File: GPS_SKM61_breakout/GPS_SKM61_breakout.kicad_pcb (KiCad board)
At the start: 2 copper layers, 49.5 x 38.1 mm, 2 parts, among them P1 CONN_01X06, U1 SKM61

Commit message: added gerbers for skm61
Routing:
- net Net-(P1-Pad6): track 0.00 -> 13.3 mm
- net Net-(P1-Pad5): track 0.00 -> 12.9 mm
- net Net-(P1-Pad1): track 0.00 -> 12.7 mm
- net Net-(P1-Pad4): track 0.00 -> 12.5 mm
- net Net-(P1-Pad2): track 0.00 -> 12.3 mm
- net Net-(P1-Pad3): track 0.00 -> 12.0 mm
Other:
- outline, holes or cut-outs redrawn
- net class Default: clearance 0.2 -> 0.8128; trace_width 0.25 -> 0.635; via_dia 0.6 -> 2.54; via_drill 0.4 -> 0.8128
- rule trace_clearance: 0.2 -> 0.8128
- rule trace_min: 0.2 -> 0.635
- rule via_min_drill: 0.3 -> 0.8128
- rule via_min_size: 0.4 -> 2.54
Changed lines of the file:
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@@
   (general
     (links 6)
-    (no_connects 6)
-    (area 0 0 0 0)
+    (no_connects 0)
+    (area 141.598867 93.904999 194.385001 132.155001)
     (thickness 1.6)
-    (drawings 4)
-    (tracks 0)
+    (drawings 8)
+    (tracks 25)
     (zones 0)
     (modules 2)
@@
   )
   (setup
-    (last_trace_width 0.25)
-    (trace_clearance 0.2)
+    (last_trace_width 1.778)
+    (user_trace_width 0.635)
+    (user_trace_width 0.762)
+    (user_trace_width 1.016)
+    (user_trace_width 1.27)
+    (user_trace_width 1.524)
+    (user_trace_width 1.778)
+    (user_trace_width 2.032)
+    (user_trace_width 2.286)
+    (trace_clearance 0.8128)
     (zone_clearance 0.508)
     (zone_45_only no)
-    (trace_min 0.2)
+    (trace_min 0.635)
     (segment_width 0.2)
     (edge_width 0.15)
-    (via_size 0.6)
-    (via_drill 0.4)
-    (via_min_size 0.4)
-    (via_min_drill 0.3)
+    (via_size 2.54)
+    (via_drill 0.8128)
+    (via_min_size 2.54)
+    (via_min_drill 0.8128)
     (uvia_size 0.3)
     (uvia_drill 0.1)
     (uvias_allowed no)
-    (uvia_min_size 0.2)
-    (uvia_min_drill 0.1)
+    (uvia_min_size 0)
+    (uvia_min_drill 0)
     (pcb_text_width 0.3)
     (pcb_text_size 1.5 1.5)
@@
     (mod_text_size 1 1)
     (mod_text_width 0.15)
-    (pad_size 1.524 1.524)
-    (pad_drill 0.762)
+    (pad_size 3 1)
+    (pad_drill 0)
     (pad_to_mask_clearance 0.2)
     (aux_axis_origin 0 0)
     (visible_elements FFFFFF7F)
     (pcbplotparams
-      (layerselection 0x00030_80000001)
+      (layerselection 0x01000_00000001)
       (usegerberextensions false)
       (excludeedgelayer true)
@@
       (outputformat 1)
       (mirror false)
-      (drillshape 1)
+      (drillshape 0)
       (scaleselection 1)
-      (outputdirectory ""))
+      (outputdirectory gerbers/))
   )
   (net 0 "")
@@
   (net 6 "Net-(P1-Pad6)")
   (net_class Default "This is the default net class."
-    (clearance 0.2)
-    (trace_width 0.25)
-    (via_dia 0.6)
-    (via_drill 0.4)
+    (clearance 0.8128)
+    (trace_width 0.635)
+    (via_dia 2.54)
+    (via_drill 0.8128)
     (uvia_dia 0.3)
     (uvia_drill 0.1)
@@
     (pad 12 smd rect (at 16 0) (size 3 1) (layers F.Cu F.Paste F.Mask))
   )
+  (gr_line (start 189.46 101.23) (end 161.96 101.23) (angle 90) (layer Edge.Cuts) (width 0.15))
+  (gr_line (start 189.46 124.33) (end 189.46 101.23) (angle 90) (layer Edge.Cuts) (width 0.15))
+  (gr_line (start 161.96 124.33) (end 189.46 124.33) (angle 90) (layer Edge.Cuts) (width 0.15))
+  (gr_line (start 161.96 101.23) (end 161.96 124.33) (angle 90) (layer Edge.Cuts) (width 0.15))
   (gr_line (start 194.31 132.08) (end 144.78 132.08) (angle 90) (layer Edge.Cuts) (width 0.15))
   (gr_line (start 194.31 93.98) (end 194.31 132.08) (angle 90) (layer Edge.Cuts) (width 0.15))
   (gr_line (start 144.78 93.98) (end 194.31 93.98) (angle 90) (layer Edge.Cuts) (width 0.15))
   (gr_line (start 144.78 132.08) (end 144.78 93.98) (angle 90) (layer Edge.Cuts) (width 0.15))
+  (segment (start 159.26 108.5) (end 157.8268 108.5) (width 1.016) (layer F.Cu) (net 1))
+  (segment (start 157.8268 108.5) (end 156.0068 106.68) (width 1.016) (layer F.Cu) (net 1))
+  (segment (start 156.0068 106.68) (end 151.13 106.68) (width 1.016) (layer F.Cu) (net 1))
+  (segment (start 151.13 106.68) (end 147.32 106.68) (width 1.778) (layer F.Cu) (net 1))
+  (segment (start 159.26 110.01) (end 155.7554 110.01) (width 1.016) (layer F.Cu) (net 2))
+  (segment (start 154.9654 109.22) (end 151.13 109.22) (width 1.016) (layer F.Cu) (net 2))
+  (segment (start 151.13 109.22) (end 147.32 109.22) (width 1.778) (layer F.Cu) (net 2))
+  (segment (start 155.7554 110.01) (end 154.9654 109.22) (width 1.016) (layer F.Cu) (net 2))
+  (segment (start 159.26 111.52) (end 153.7716 111.506) (width 1.016) (layer F.Cu) (net 3))
+  (segment (start 153.5316 111.746) (end 150.495 111.76) (width 1.016) (layer F.Cu) (net 3))
+  (segment (start 150.495 111.76) (end 147.32 111.76) (width 1.778) (layer F.Cu) (net 3))
+  (segment (start 153.7716 111.506) (end 153.5316 111.746) (width 1.016) (layer F.Cu) (net 3))
+  (segment (start 159.26 113.03) (end 154.3812 113.03) (width 1.016) (layer F.Cu) (net 4))
+  (segment (start 153.1112 114.3) (end 150.495 114.3) (width 1.016) (layer F.Cu) (net 4))
+  (segment (start 150.495 114.3) (end 147.32 114.3) (width 1.778) (layer F.Cu) (net 4))
+  (segment (start 154.3812 113.03) (end 153.1112 114.3) (width 1.016) (layer F.Cu) (net 4))
+  (segment (start 159.26 114.54) (end 155.335 114.54) (width 1.016) (layer F.Cu) (net 5))
+  (segment (start 153.035 116.84) (end 150.495 116.84) (width 1.016) (layer F.Cu) (net 5))
+  (segment (start 150.495 116.84) (end 147.32 116.84) (width 1.778) (layer F.Cu) (net 5))
+  (segment (start 155.335 114.54) (end 153.035 116.84) (width 1.016) (layer F.Cu) (net 5))
+  (segment (start 159.26 114.54) (end 159.246 114.554) (width 0.635) (layer F.Cu) (net 5))
+  (segment (start 159.26 116.05) (end 156.5174 116.05) (width 1.016) (layer F.Cu) (net 6))
+  (segment (start 153.1874 119.38) (end 150.495 119.38) (width 1.016) (layer F.Cu) (net 6))
+  (segment (start 150.495 119.38) (end 147.32 119.38) (width 1.778) (layer F.Cu) (net 6))
+  (segment (start 156.5174 116.05) (end 153.1874 119.38) (width 1.016) (layer F.Cu) (net 6))
 )

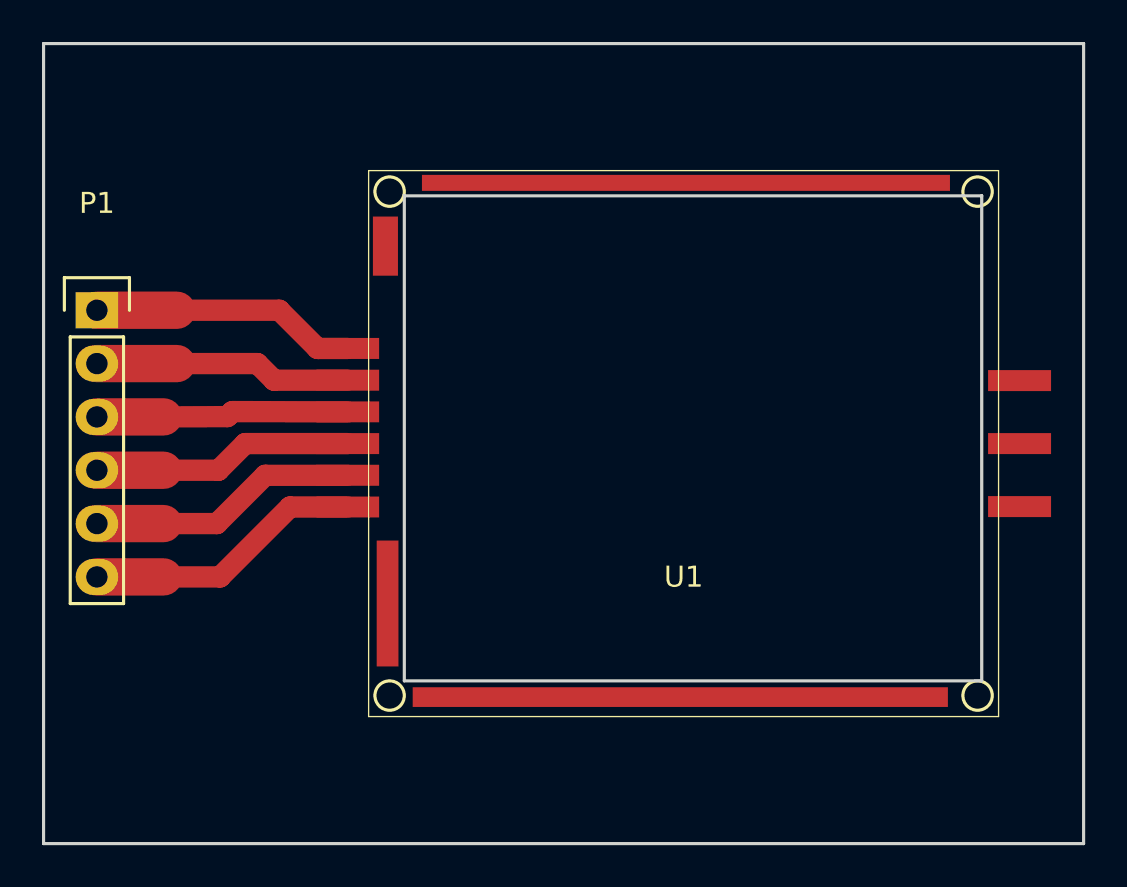
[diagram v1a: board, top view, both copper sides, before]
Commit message: added a few more breakout board projects
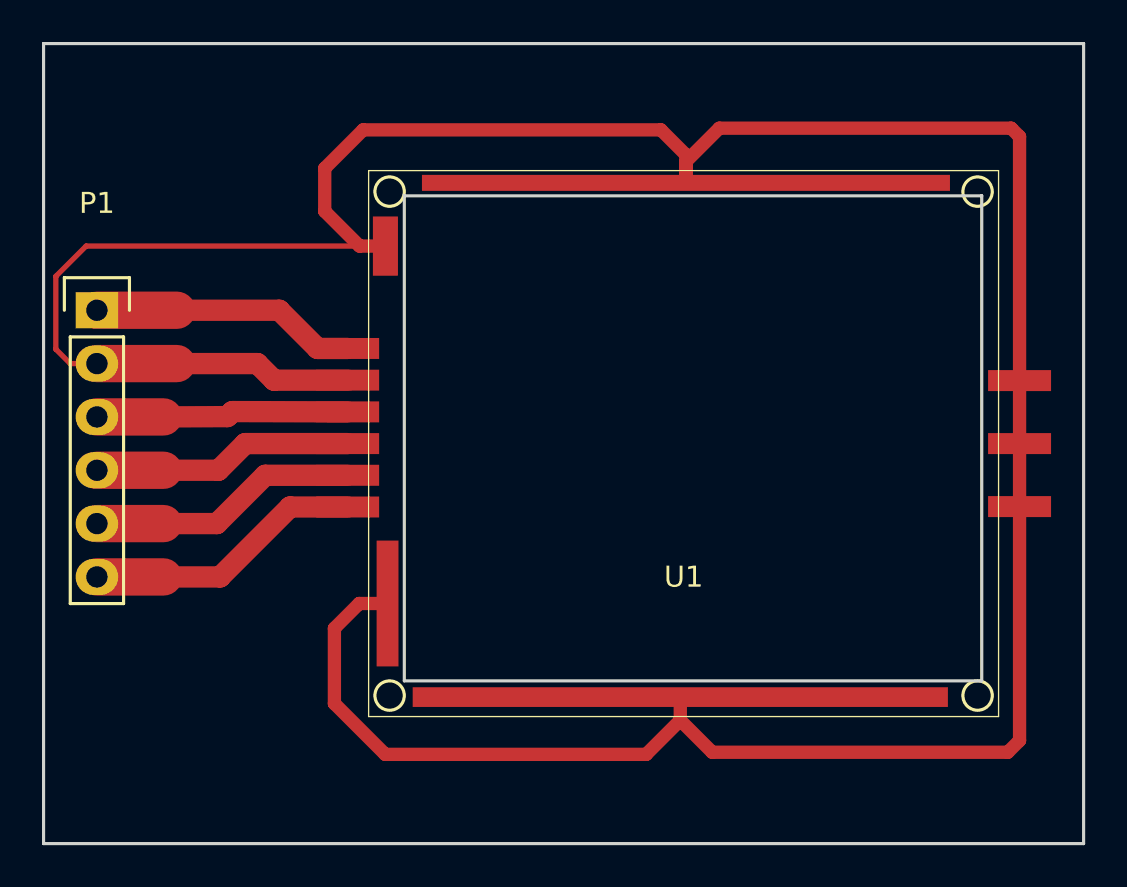
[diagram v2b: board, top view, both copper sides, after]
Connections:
- net Net-(P1-Pad1) renamed PPS
- net Net-(P1-Pad3) renamed +3V3
- net Net-(P1-Pad4) renamed VBAT
- net Net-(P1-Pad5) renamed RXD
- net Net-(P1-Pad6) renamed TXD
- P1 pad 2: Net-(P1-Pad2) -> GND
- U1 pad 10: (no net) -> GND
- U1 pad 11: (no net) -> GND
- U1 pad 12: (no net) -> GND
- U1 pad 13: (no net) -> GND
- U1 pad 5: Net-(P1-Pad2) -> GND
- U1 pad 7: (no net) -> GND
- U1 pad 8: (no net) -> GND
- U1 pad 9: (no net) -> GND
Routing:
- net GND: track 0.00 -> 149.0 mm
- net Net-(P1-Pad2): track 12.3 -> 0.00 mm
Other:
- rule trace_min: 0.635 -> 0.254
